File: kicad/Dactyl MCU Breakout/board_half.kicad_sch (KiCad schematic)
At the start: 19 parts, among them J1 Columns, J2 Rows, J3 Thumbs, J5 Display, J6 External, J7 JST, J8 Split, J9 Vic, SW1 Battery, SW2 Reset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

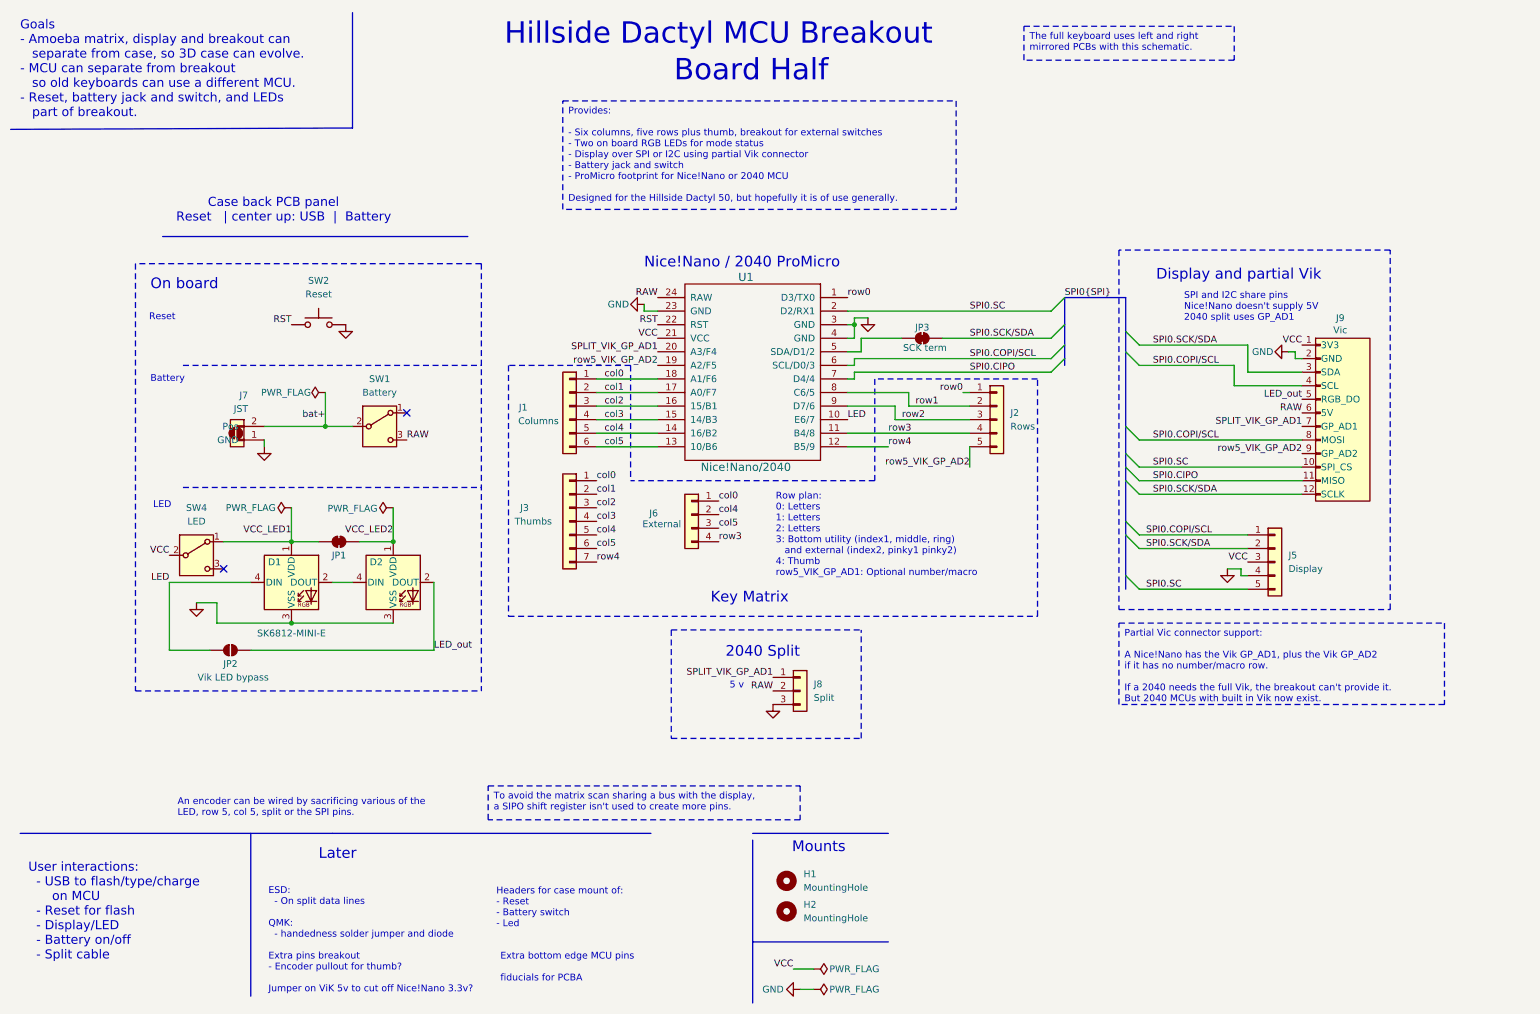
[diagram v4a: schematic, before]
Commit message: feat: split USB-C
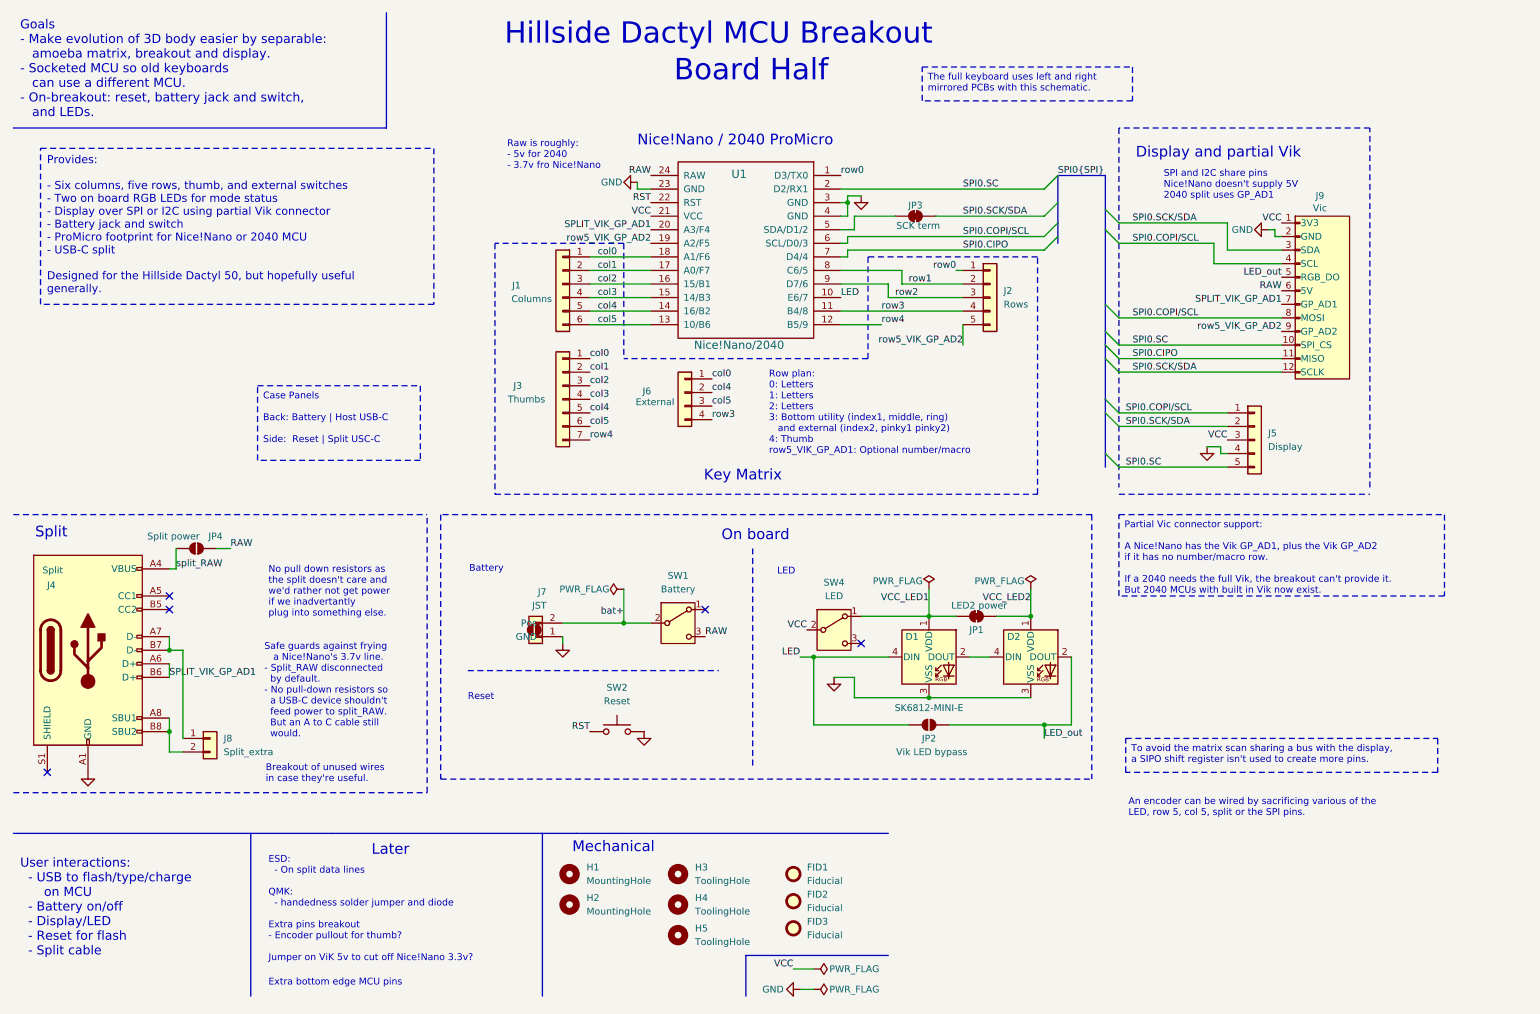
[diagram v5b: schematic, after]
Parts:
- removed J8: Split, Connector_PinHeader_2.54mm:PinHeader_1x03_P2.54mm_Vertical, symbol Connector_Generic:Conn_01x03
- added FID1, FID2, FID3: Fiducial, Fiducial:Fiducial_1mm_Mask2mm, symbol Mechanical:Fiducial
- added H3, H4, H5: ToolingHole, Dactyl:ToolingHole_1.152mm, symbol Mechanical:MountingHole
- added J4: Split, Connector_USB:USB_C_Receptacle_HRO_TYPE-C-31-M-12, symbol Connector:USB_C_Receptacle_USB2.0_16P
- added J8: Split_extra, Connector_PinHeader_2.54mm:PinHeader_1x02_P2.54mm_Vertical, symbol Connector_Generic:Conn_01x02
- added JP4: Split power, Jumper:SolderJumper-2_P1.3mm_Open_RoundedPad1.0x1.5mm, symbol Jumper:SolderJumper_2_Open
- JP1: value LED2 cutoff -> LED2 power
- U1: footprint Dactyl:ProMicro_v2_1 -> Dactyl:ProMicro_v2_1S
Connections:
- net GND: now also J4.A1 (GND), J4.A12 (GND), J4.B1 (GND), J4.B12 (GND)
- net RAW: now also JP4.2 (B)
- net SPLIT_VIK_GP_AD1: now also J4.A6 (D+), J4.B6 (D+)
- new net: J4.A7 (D-), J4.B7 (D-), J8.1 (Pin_1)
- new net: J4.A8 (SBU1), J4.B8 (SBU2), J8.2 (Pin_2)
- new net split_RAW: J4.A4 (VBUS), J4.A9 (VBUS), J4.B4 (VBUS), J4.B9 (VBUS), JP4.1 (A)
- no-connect marks 2 -> 5
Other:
- note added: "Breakout of unused wires in case they're useful."
- note added: "Extra bottom edge MCU pins"
- note added: "Goals - Make evolution of 3D body easier by separable: amoeba matrix, breakout and display. - Socketed MCU so old keyboards can use a different MCU. - On-breakout: reset, battery jack and switch, and LEDs."
- note added: "Mechanical"
- note added: "No pull down resistors as the split doesn't care and we'd rather not get power if we inadvertantly plug into something else."
- note added: "Raw is roughly: - 5v for 2040 - 3.7v fro Nice!Nano"
- note added: "Safe guards against frying a Nice!Nano's 3.7v line. - Split_RAW disconnected by default. - No pull-down resistors so a USB-C device shouldn't feed power to split_RAW. But an A to C cable still would."
- note added: "Split"
- note added: "User interactions: - USB to flash/type/charge on MCU - Battery on/off - Display/LED - Reset for flash - Split cable"
- note removed: "2040 Split"
- note removed: "5 v"
- note removed: "Case back PCB panel Reset | center up: USB | Battery"
- note removed: "Extra bottom edge MCU pins fiducials for PCBA"
- note removed: "Goals - Amoeba matrix, display and breakout can separate from case, so 3D case can evolve. - MCU can separate from breakout so old keyboards can use a different MCU. - Reset, battery jack and switch, and LEDs part of breakout."
- note removed: "Headers for case mount of: - Reset - Battery switch - Led"
- note removed: "Mounts"
- note removed: "User interactions: - USB to flash/type/charge on MCU - Reset for flash - Display/LED - Battery on/off - Split cable"
- moved on the sheet: D1, D2, H1, H2, J1, J2, J3, J5, J6, J7, J9, JP1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

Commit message: feat(schematic): use Config field DNF for non PCBA
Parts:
- D1, D2, FID1, FID2, FID3, H1, H2, H3, H4, H5, J1, J2, J3, J5, J6, J8, JP1, JP2, JP3, JP4, U1: Config (none) -> DNF
- J4, J9: JLC PCBA Type (none) -> Economic
- SW1, SW4: JLC PCBA Type (none) -> Standard

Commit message: feat: rename LCSC part column
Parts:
- J4: LCSC Part (none) -> C165948; LCSC Part # C165948 -> (none)
- J9: LCSC Part (none) -> C2906115; LCSC Part # C2906115 -> (none)
- SW1, SW4: LCSC Part (none) -> C221662; LCSC Part # C221662 -> (none)
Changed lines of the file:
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@@
-			)
-		)
-		(property "LCSC Part #" "C221662"
-			(at 137.16 127 0)
-			(effects
-				(font
-					(size 1.27 1.27)
-				)
-				(hide yes)
 			)
 		)
@@
 			)
 		)
+		(property "LCSC Part" "C221662"
+			(at 137.16 127 0)
+			(effects
+				(font
+					(size 1.27 1.27)
+				)
+				(hide yes)
+			)
+		)
 		(pin "2"
 		)
@@
 			)
 		)
-		(property "LCSC Part #" "C2906115"
-			(at 257.81 64.77 0)
-			(effects
-				(font
-					(size 1.27 1.27)
-				)
-				(hide yes)
-			)
-		)
 		(property "JLC PCBA Type" "Economic"
 			(at 257.81 64.77 0)
@@
 		)
 		(property "Config" ""
+			(at 257.81 64.77 0)
+			(effects
+				(font
+					(size 1.27 1.27)
+				)
+				(hide yes)
+			)
+		)
+		(property "LCSC Part" "C2906115"
 			(at 257.81 64.77 0)
 			(effects
@@
 			)
 		)
-		(property "LCSC Part #" "C221662"
-			(at 166.37 128.27 0)
-			(effects
-				(font
-					(size 1.27 1.27)
-				)
-				(hide yes)
-			)
-		)
 		(property "JLC PCBA Type" "Standard"
 			(at 166.37 128.27 0)
@@
 		)
 		(property "Config" ""
+			(at 166.37 128.27 0)
+			(effects
+				(font
+					(size 1.27 1.27)
+				)
+				(hide yes)
+			)
+		)
+		(property "LCSC Part" "C221662"
 			(at 166.37 128.27 0)
 			(effects
@@
 			)
 		)
-		(property "LCSC Part #" "C165948"
-			(at 26.67 132.08 0)
-			(effects
-				(font
-					(size 1.27 1.27)
-				)
-				(hide yes)
-			)
-		)
 		(property "JLC PCBA Type" "Economic"
 			(at 26.67 132.08 0)
@@
 			(at 26.67 132.08 0)
 			(effects
+				(font
+					(size 1.27 1.27)
+				)
+				(hide yes)
+			)
+		)
+		(property "LCSC Part" "C165948"
+			(at 26.67 132.08 0)
+			(effects

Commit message: doc: schema doc cleanup
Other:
- note added: "Breakout of unused wires in case we find a use."
- note removed: "Breakout of unused wires in case they're useful."
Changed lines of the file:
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@@
 		)
 	)
-	(text "Breakout of unused wires \nin case they're useful."
+	(text "Breakout of unused wires \nin case we find a use."
 		(exclude_from_sim no)
 		(at 59.944 156.972 0)
